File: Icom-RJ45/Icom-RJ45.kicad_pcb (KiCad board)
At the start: 2 copper layers, 27.3 x 30.5 mm, 6 parts, among them J1 Mic Input, J2 Base Board, J3 Headphone/Speaker Input

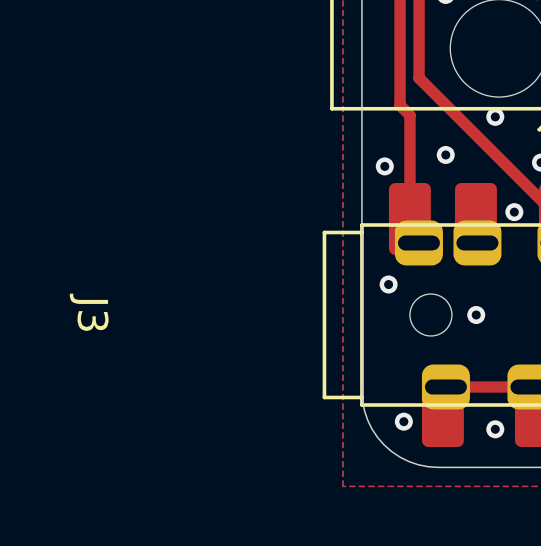
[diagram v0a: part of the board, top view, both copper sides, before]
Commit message: Added an Interactive BOM for the Base Board assembly.
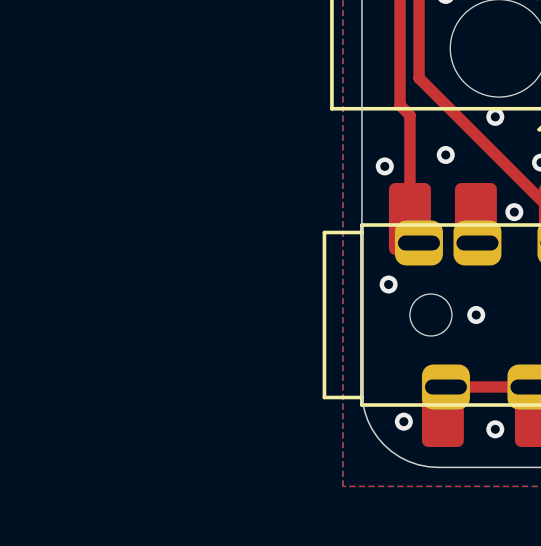
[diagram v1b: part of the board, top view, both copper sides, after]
